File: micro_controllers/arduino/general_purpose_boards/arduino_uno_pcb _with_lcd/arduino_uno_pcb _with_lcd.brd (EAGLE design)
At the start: 102.5 x 90.2 mm, 25 parts, among them IC1 ATMEGA328, IC2 7805, Q1 16MHZ

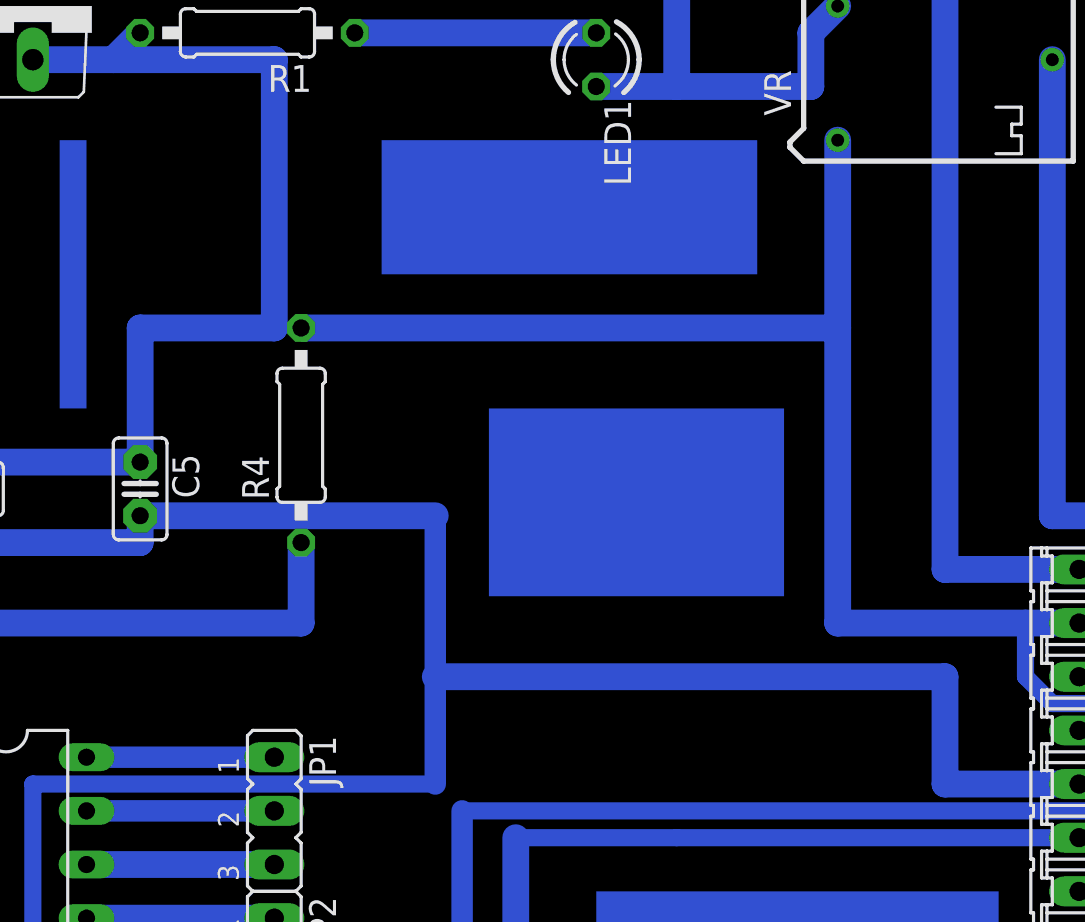
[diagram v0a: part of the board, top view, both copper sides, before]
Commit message: 
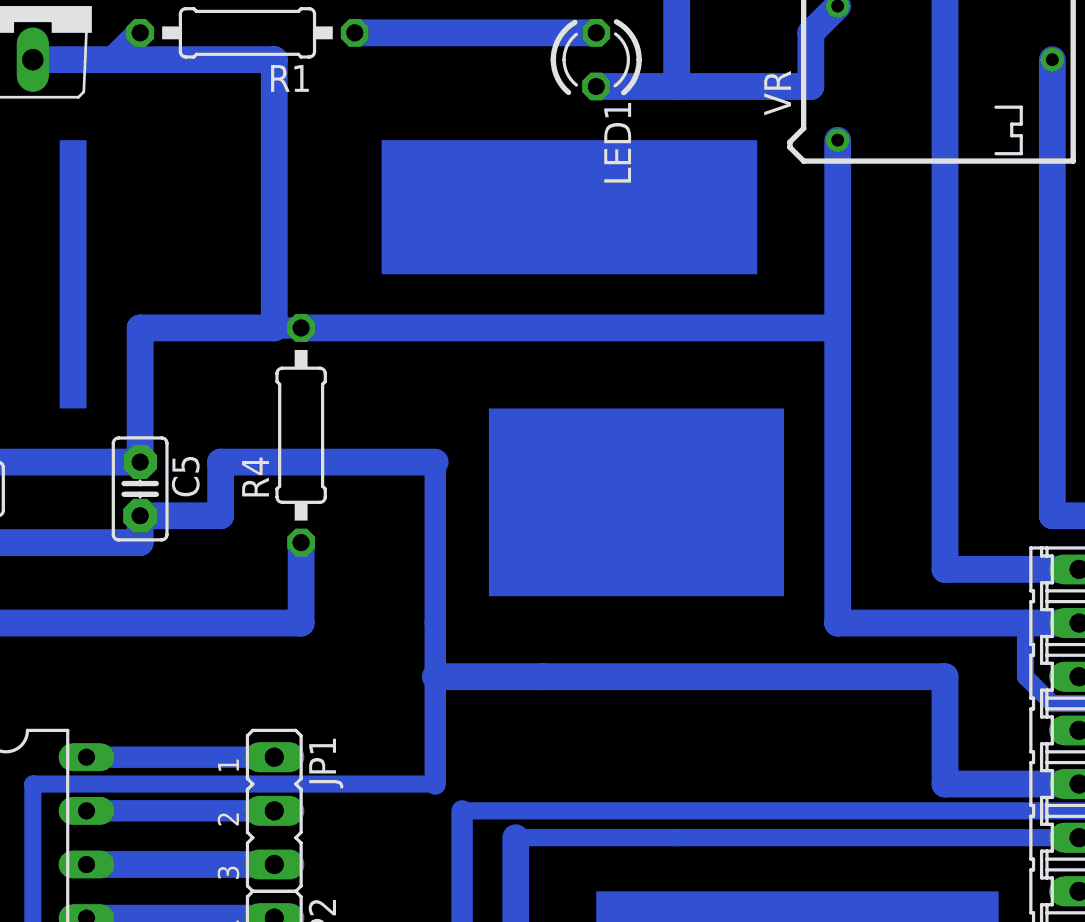
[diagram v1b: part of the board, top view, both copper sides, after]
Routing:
- net N$5: track 477.6 -> 490.3 mm
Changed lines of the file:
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@@
 <?xml version="1.0" encoding="utf-8"?>
 <!DOCTYPE eagle SYSTEM "eagle.dtd">
-<eagle version="6.1">
+<eagle version="7.1.0">
 <drawing>
 <settings>
@@
 </class>
 </classes>
-<designrules>
+<designrules name="default">
 <description language="de">&lt;b&gt;EAGLE Design Rules&lt;/b&gt;
 &lt;p&gt;
@@
 <pass name="Default">
 <param name="RoutingGrid" value="50mil"/>
+<param name="AutoGrid" value="1"/>
+<param name="Efforts" value="0"/>
+<param name="TopRouterVariant" value="1"/>
 <param name="tpViaShape" value="round"/>
 <param name="PrefDir.1" value="0"/>
@@
 <wire x1="92.71" y1="45.72" x2="92.71" y2="40.64" width="1.27" layer="16"/>
 <wire x1="92.71" y1="40.64" x2="99.06" y2="40.64" width="1.27" layer="16"/>
-<wire x1="68.58" y1="45.72" x2="92.71" y2="45.72" width="1.27" layer="16"/>
-<wire x1="54.61" y1="53.34" x2="68.58" y2="53.34" width="1.27" layer="16"/>
+<wire x1="68.58" y1="45.72" x2="73.66" y2="45.72" width="1.27" layer="16"/>
+<wire x1="73.66" y1="45.72" x2="92.71" y2="45.72" width="1.27" layer="16"/>
+<wire x1="54.61" y1="53.34" x2="58.42" y2="53.34" width="1.27" layer="16"/>
+<wire x1="58.42" y1="53.34" x2="58.42" y2="55.88" width="1.27" layer="16"/>
+<wire x1="58.42" y1="55.88" x2="68.58" y2="55.88" width="1.27" layer="16"/>
 <wire x1="46.99" y1="63.5" x2="46.99" y2="74.93" width="1.27" layer="16"/>
 <wire x1="44.45" y1="54.61" x2="44.45" y2="63.5" width="1.27" layer="16"/>
@@
 <wire x1="49.53" y1="30.48" x2="49.53" y2="26.67" width="0.8128" layer="16"/>
 <wire x1="68.58" y1="40.64" x2="49.53" y2="40.64" width="0.8128" layer="16"/>
-<wire x1="68.58" y1="53.34" x2="68.58" y2="40.64" width="1.016" layer="16"/>
+<wire x1="68.58" y1="55.88" x2="68.58" y2="48.26" width="1.016" layer="16"/>
+<wire x1="68.58" y1="48.26" x2="68.58" y2="40.64" width="1.016" layer="16"/>
 <wire x1="80.01" y1="78.74" x2="80.01" y2="73.66" width="1.27" layer="16"/>
 <wire x1="46.99" y1="78.74" x2="80.01" y2="78.74" width="1.27" layer="16"/>
 <wire x1="46.99" y1="74.93" x2="46.99" y2="78.74" width="1.27" layer="16"/>
+<wire x1="73.66" y1="45.72" x2="68.58" y2="45.72" width="0.4064" layer="16"/>
+<wire x1="68.58" y1="45.72" x2="68.58" y2="48.26" width="0.4064" layer="16"/>
 </signal>
 <signal name="N$7">
@@
 <wire x1="60.96" y1="62.23" x2="54.61" y2="62.23" width="1.27" layer="16"/>
 <wire x1="54.61" y1="62.23" x2="54.61" y2="55.88" width="1.27" layer="16"/>
-<wire x1="62.23" y1="62.23" x2="60.96" y2="62.23" width="0.508" layer="16"/>
+<wire x1="62.23" y1="62.23" x2="60.96" y2="62.23" width="1.016" layer="16"/>
 <wire x1="48.26" y1="26.67" x2="48.26" y2="24.13" width="0.8128" layer="16"/>
 <wire x1="48.26" y1="24.13" x2="49.53" y2="24.13" width="0.8128" layer="16"/>
@@
 <wire x1="102.87" y1="24.13" x2="80.01" y2="24.13" width="0.8128" layer="16"/>
 <wire x1="80.01" y1="24.13" x2="80.01" y2="12.7" width="0.8128" layer="16"/>
-<wire x1="87.63" y1="48.26" x2="87.63" y2="71.12" width="1.27" layer="16"/>
+<wire x1="87.63" y1="48.26" x2="87.63" y2="62.23" width="1.27" layer="16"/>
+<wire x1="87.63" y1="62.23" x2="87.63" y2="71.12" width="1.27" layer="16"/>
 <wire x1="96.52" y1="48.26" x2="87.63" y2="48.26" width="1.27" layer="16"/>
 </signal>
